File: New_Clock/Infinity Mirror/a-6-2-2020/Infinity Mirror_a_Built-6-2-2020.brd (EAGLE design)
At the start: 81 x 26 mm, 20 parts, among them IC1 MSGEQ7P, J1 Vsupply, J3 LED, J4 LED_CAP, U1 DS1307, Y1 32.768kHz

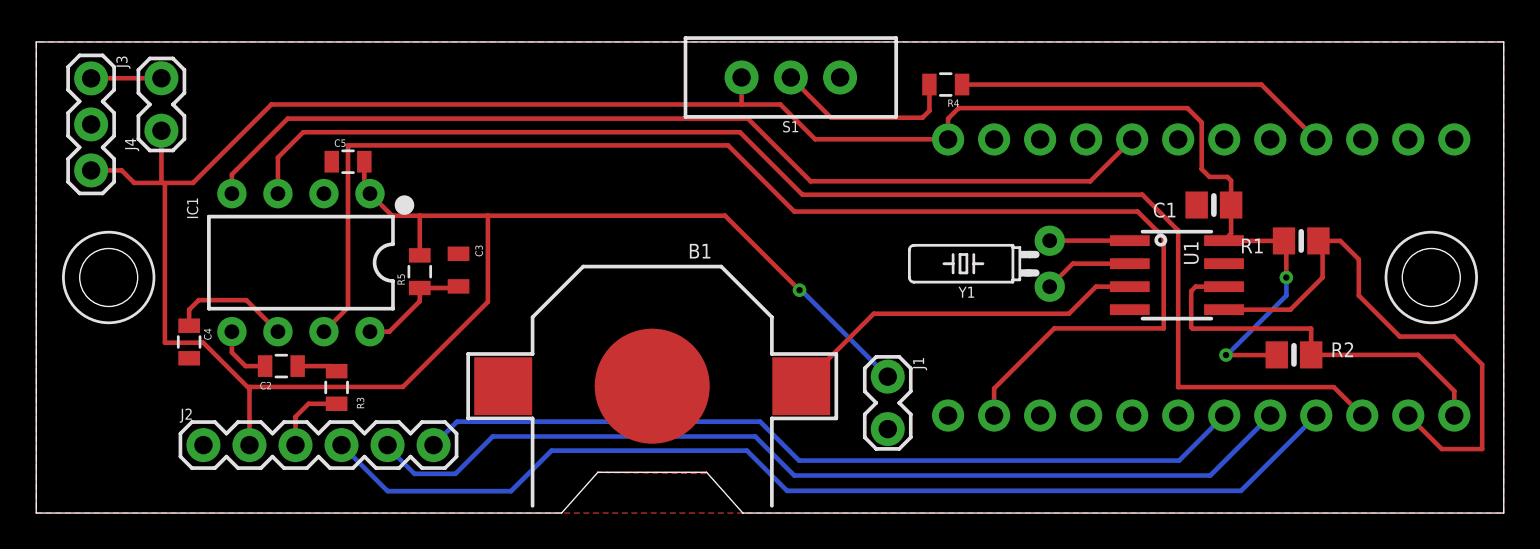
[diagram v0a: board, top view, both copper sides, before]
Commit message: added test code for board-a proving that the clock, 3 analog inputs, daylight-savings time switch and msgeq7 and leds work
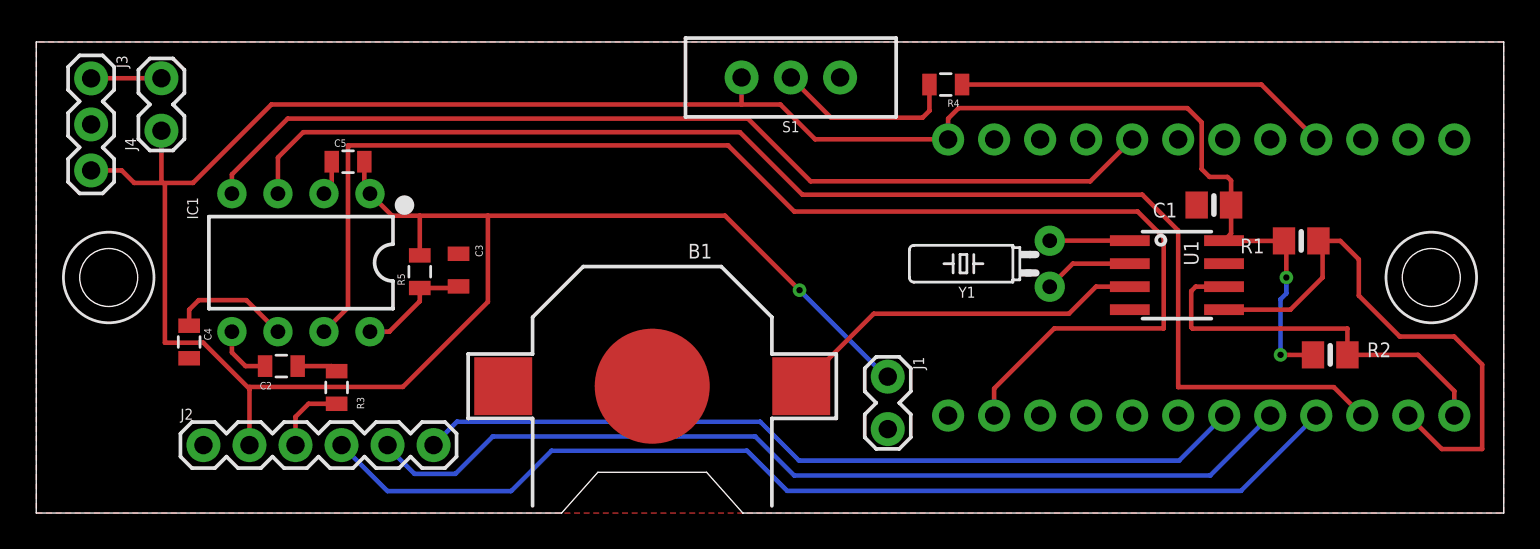
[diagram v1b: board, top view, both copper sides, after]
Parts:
- J2: value (none) -> AUDIO_POTS
- moved R2 2.00 mm to (71.4, 8.73)
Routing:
- net VCC: track 166.8 -> 164.3 mm
- net XO: track 6.95 -> 4.95 mm
- net GND: track 4.49 -> 5.82 mm
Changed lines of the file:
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@@
 <layer number="16" name="Bottom" color="1" fill="1" visible="yes" active="yes"/>
 <layer number="17" name="Pads" color="2" fill="1" visible="yes" active="yes"/>
-<layer number="18" name="Vias" color="2" fill="1" visible="no" active="yes"/>
+<layer number="18" name="Vias" color="2" fill="1" visible="yes" active="yes"/>
 <layer number="19" name="Unrouted" color="6" fill="1" visible="yes" active="yes"/>
 <layer number="20" name="Dimension" color="24" fill="1" visible="yes" active="yes"/>
-<layer number="21" name="tPlace" color="7" fill="1" visible="no" active="yes"/>
+<layer number="21" name="tPlace" color="7" fill="1" visible="yes" active="yes"/>
 <layer number="22" name="bPlace" color="7" fill="1" visible="yes" active="yes"/>
 <layer number="23" name="tOrigins" color="15" fill="1" visible="yes" active="yes"/>
 <layer number="24" name="bOrigins" color="15" fill="1" visible="yes" active="yes"/>
-<layer number="25" name="tNames" color="7" fill="1" visible="no" active="yes"/>
+<layer number="25" name="tNames" color="7" fill="1" visible="yes" active="yes"/>
 <layer number="26" name="bNames" color="7" fill="1" visible="no" active="yes"/>
-<layer number="27" name="tValues" color="7" fill="1" visible="no" active="yes"/>
+<layer number="27" name="tValues" color="7" fill="1" visible="yes" active="yes"/>
 <layer number="28" name="bValues" color="7" fill="1" visible="no" active="yes"/>
 <layer number="29" name="tStop" color="7" fill="3" visible="yes" active="yes"/>
-<layer number="30" name="bStop" color="7" fill="6" visible="no" active="yes"/>
+<layer number="30" name="bStop" color="7" fill="6" visible="yes" active="yes"/>
 <layer number="31" name="tCream" color="7" fill="4" visible="no" active="yes"/>
 <layer number="32" name="bCream" color="7" fill="5" visible="no" active="yes"/>
@@
 <layer number="42" name="bRestrict" color="1" fill="10" visible="yes" active="yes"/>
 <layer number="43" name="vRestrict" color="2" fill="10" visible="yes" active="yes"/>
-<layer number="44" name="Drills" color="7" fill="1" visible="no" active="yes"/>
+<layer number="44" name="Drills" color="7" fill="1" visible="yes" active="yes"/>
 <layer number="45" name="Holes" color="7" fill="1" visible="yes" active="yes"/>
 <layer number="46" name="Milling" color="3" fill="1" visible="no" active="yes"/>
@@
 </class>
 </classes>
-<designrules name="default">
+<designrules name="default *">
 <description language="de">&lt;b&gt;EAGLE Design Rules&lt;/b&gt;
 &lt;p&gt;
@@
 <param name="checkNames" value="1"/>
 <param name="checkWireStubs" value="1"/>
-<param name="checkPolygonWidth" value="0"/>
+<param name="checkPolygonWidth" value="1"/>
 <param name="useDiameter" value="13"/>
 <param name="maxErrors" value="50"/>
@@
 <attribute name="VALUE" x="44.968" y="8.62" size="0.6096" layer="27" font="vector" ratio="20" rot="R270"/>
 </element>
-<element name="R2" library="microbuilder" package="0805-NO" value="10K" x="69.42" y="8.73" smashed="yes">
-<attribute name="NAME" x="71.452" y="8.603" size="0.8128" layer="25" ratio="18"/>
-<attribute name="VALUE" x="71.452" y="7.968" size="0.4064" layer="27" ratio="10"/>
+<element name="R2" library="microbuilder" package="0805-NO" value="10K" x="71.42" y="8.73" smashed="yes">
+<attribute name="NAME" x="73.452" y="8.603" size="0.8128" layer="25" ratio="18"/>
+<attribute name="VALUE" x="73.452" y="7.968" size="0.4064" layer="27" ratio="10"/>
 </element>
 <element name="R1" library="microbuilder" package="0805-NO" value="10K" x="69.82" y="15.02" smashed="yes" rot="R180">
@@
 <attribute name="VALUE" x="13.704" y="6.923" size="0.4064" layer="27"/>
 </element>
-<element name="J2" library="SparkFun-Connectors" library_urn="urn:adsk.eagle:library:513" package="1X06" package3d_urn="urn:adsk.eagle:package:38009/1" value="" x="9.23" y="3.75" smashed="yes">
+<element name="J2" library="SparkFun-Connectors" library_urn="urn:adsk.eagle:library:513" package="1X06" package3d_urn="urn:adsk.eagle:package:38009/1" value="AUDIO_POTS" x="9.23" y="3.75" smashed="yes">
 <attribute name="NAME" x="7.96" y="5.147" size="0.6096" layer="25" font="vector" ratio="20"/>
 <attribute name="PROD_ID" value="CONN-08437" x="9.23" y="3.75" size="1.778" layer="27" display="off"/>
@@
 <contactref element="C5" pad="1"/>
 <contactref element="J3" pad="1"/>
-<wire x1="16.3" y1="19.38" x2="16.31" y2="19.39" width="0.1524" layer="1"/>
 <contactref element="U$1" pad="TG"/>
 <contactref element="S1" pad="3"/>
@@
 <wire x1="3.0378" y1="23.9978" x2="3.03" y2="23.99" width="0.1524" layer="1"/>
 <contactref element="IC1" pad="2"/>
-<wire x1="15.88" y1="17.63" x2="16.3" y2="18.05" width="0.254" layer="1"/>
-<polygon width="0" layer="1">
-<vertex x="30.95" y="2.24"/>
-<vertex x="36.92" y="2.24"/>
-<vertex x="36.98" y="2.18"/>
-</polygon>
-<polygon width="0" layer="1">
-<vertex x="0" y="26"/>
-<vertex x="0" y="0"/>
+<polygon width="0.127" layer="1">
+<vertex x="0.01" y="26"/>
+<vertex x="0.01" y="0"/>
 <vertex x="81" y="0"/>
 <vertex x="81" y="26"/>
 </polygon>
+<wire x1="15.88" y1="17.63" x2="16.31" y2="18.06" width="0.254" layer="1" curve="90"/>
+<wire x1="16.31" y1="18.06" x2="16.31" y2="19.39" width="0.254" layer="1"/>
 </signal>
 <signal name="VCC">
@@
 <wire x1="18.42" y1="17.63" x2="19.64" y2="16.41" width="0.254" layer="1"/>
 <wire x1="24.93" y1="11.6567125" x2="20.2332875" y2="6.96" width="0.254" layer="1"/>
-<wire x1="47" y1="7.5278" x2="42.2278" y2="12.3" width="0.254" layer="16"/>
-<wire x1="42.2278" y1="12.3" x2="42.13" y2="12.3" width="0.1524" layer="16"/>
+<wire x1="47" y1="7.5278" x2="46.9022" y2="7.5278" width="0.254" layer="16"/>
+<wire x1="46.9022" y1="7.5278" x2="42.13" y2="12.3" width="0.254" layer="16"/>
 <via x="42.13" y="12.3" extent="1-16" drill="0.35"/>
 <wire x1="42.13" y1="12.3" x2="38.02" y2="16.41" width="0.254" layer="1"/>
@@
 <wire x1="65.56" y1="15.035" x2="65.575" y2="15.02" width="0.254" layer="1"/>
 <wire x1="65.575" y1="15.02" x2="68.87" y2="15.02" width="0.254" layer="1"/>
-<wire x1="68.87" y1="15.02" x2="69" y2="15.15" width="0.254" layer="1"/>
 <wire x1="65.95" y1="17" x2="65.95" y2="15.425" width="0.254" layer="1"/>
 <wire x1="65.95" y1="15.425" x2="65.56" y2="15.035" width="0.254" layer="1"/>
@@
 <wire x1="69" y1="14.89" x2="69" y2="13" width="0.254" layer="1"/>
 <via x="69" y="13" extent="1-16" drill="0.35"/>
-<wire x1="69" y1="13" x2="69" y2="12" width="0.254" layer="16"/>
-<wire x1="65.72" y1="8.72" x2="65.67" y2="8.72" width="0.254" layer="16"/>
-<via x="65.67" y="8.72" extent="1-16" drill="0.35"/>
-<wire x1="65.67" y1="8.72" x2="68.46" y2="8.72" width="0.254" layer="1"/>
-<wire x1="68.46" y1="8.72" x2="68.47" y2="8.73" width="0.254" layer="1"/>
-<wire x1="69" y1="12" x2="65.72" y2="8.72" width="0.254" layer="16"/>
+<wire x1="69" y1="13" x2="69" y2="12.12" width="0.254" layer="16"/>
+<wire x1="69" y1="12.12" x2="68.68" y2="11.8" width="0.254" layer="16"/>
+<wire x1="68.68" y1="11.8" x2="68.68" y2="8.73" width="0.254" layer="16"/>
+<via x="68.68" y="8.73" extent="1-16" drill="0.35"/>
+<wire x1="68.68" y1="8.73" x2="70.46" y2="8.72" width="0.254" layer="1"/>
+<wire x1="70.46" y1="8.72" x2="70.47" y2="8.73" width="0.254" layer="1"/>
 <wire x1="64.7576" y1="18.55" x2="65.75" y2="18.55" width="0.254" layer="1"/>
 <wire x1="65.75" y1="18.55" x2="65.95" y2="18.35" width="0.254" layer="1"/>
@@
 <contactref element="R2" pad="2"/>
 <contactref element="U1" pad="6"/>
-<wire x1="76.27" y1="8.73" x2="70.37" y2="8.73" width="0.254" layer="1"/>
+<wire x1="76.27" y1="8.73" x2="72.37" y2="8.73" width="0.254" layer="1"/>
 <contactref element="U$1" pad="TA5"/>
 <wire x1="76.27" y1="8.73" x2="78.27" y2="6.73" width="0.254" layer="1"/>
@@
 <wire x1="63.995" y1="12.495" x2="63.75" y2="12.25" width="0.254" layer="1"/>
 <wire x1="63.75" y1="12.25" x2="63.75" y2="10.25" width="0.254" layer="1"/>
-<wire x1="70.37" y1="8.73" x2="70.37" y2="10.18" width="0.254" layer="1"/>
-<wire x1="70.37" y1="10.18" x2="63.82" y2="10.18" width="0.254" layer="1"/>
+<wire x1="72.37" y1="8.73" x2="72.37" y2="10.18" width="0.254" layer="1"/>
+<wire x1="72.37" y1="10.18" x2="63.82" y2="10.18" width="0.254" layer="1"/>
 <wire x1="63.82" y1="10.18" x2="63.75" y2="10.25" width="0.254" layer="1"/>
 </signal>
@@
 <signal name="XO">
 <contactref element="U1" pad="2"/>
-<wire x1="60.36" y1="13.765" x2="58.36" y2="13.765" width="0.1524" layer="1"/>
 <contactref element="Y1" pad="1"/>
-<wire x1="60.36" y1="13.765" x2="57.215" y2="13.765" width="0.254" layer="1"/>
-<wire x1="57.215" y1="13.765" x2="55.94" y2="12.49" width="0.254" layer="1"/>
+<wire x1="55.94" y1="12.49" x2="57.215" y2="13.765" width="0.254" layer="1"/>
+<wire x1="57.215" y1="13.765" x2="60.36" y2="13.765" width="0.254" layer="1"/>
 </signal>
 <signal name="8-CKIN">
@@
 <contactref element="R3" pad="1"/>
 <contactref element="C2" pad="2"/>
-<wire x1="16.58" y1="7.83" x2="16.63" y2="7.88" width="0.1524" layer="1"/>
-<wire x1="16.58" y1="7.83" x2="16.52" y2="7.77" width="0.254" layer="1"/>
 <wire x1="14.43" y1="8.11" x2="16.3" y2="8.11" width="0.254" layer="1"/>
 <wire x1="16.3" y1="8.11" x2="16.58" y2="7.83" width="0.254" layer="1"/>
